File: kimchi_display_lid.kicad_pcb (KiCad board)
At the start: 4 copper layers, 147 x 77 mm, 22 parts, among them J1 DF40HC(3.5)-60DS, J2 DF40HC(3.5)-60DS, J3 H19C-6S-0.5SH, J4 FH19C-40S-0.5SH(10), U1 24C32, U2 AP3019AKTR-G1

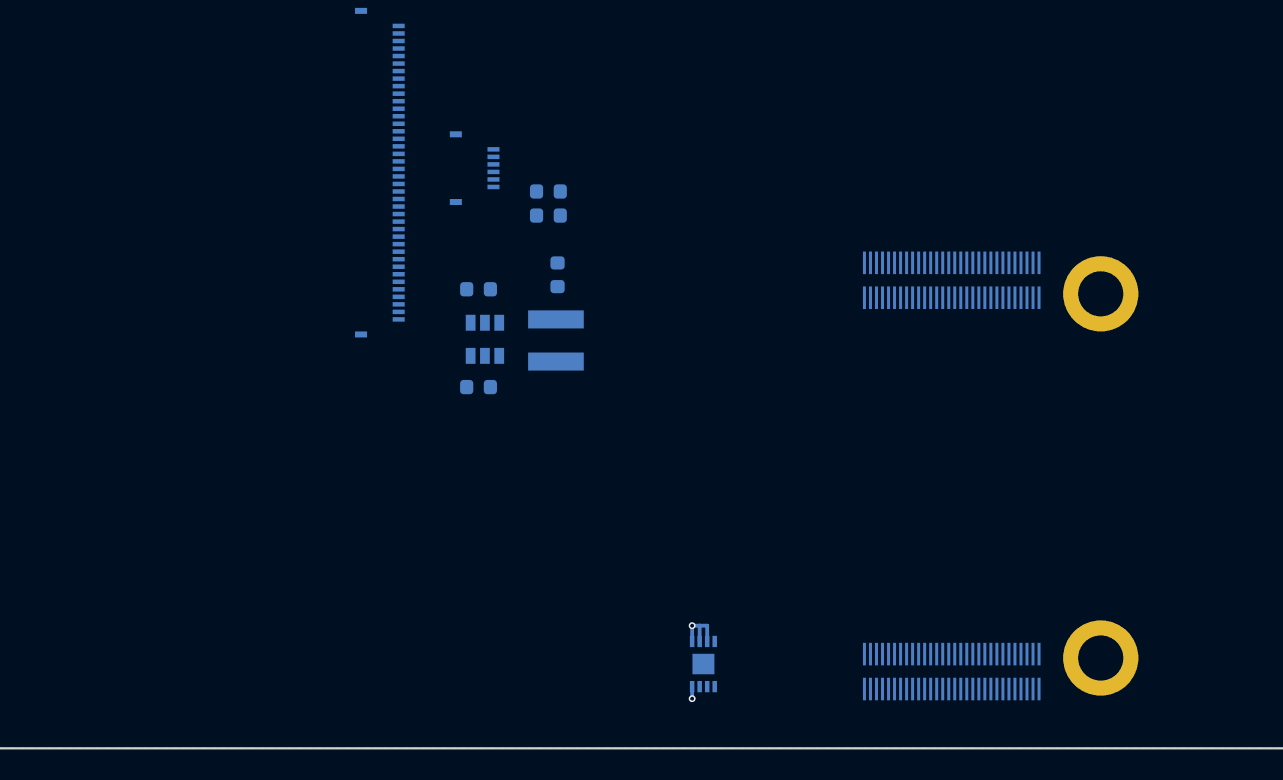
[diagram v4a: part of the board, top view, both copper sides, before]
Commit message: Add level translator and route
Signed-off-by: Michael Welling <mwelling@ieee.org>
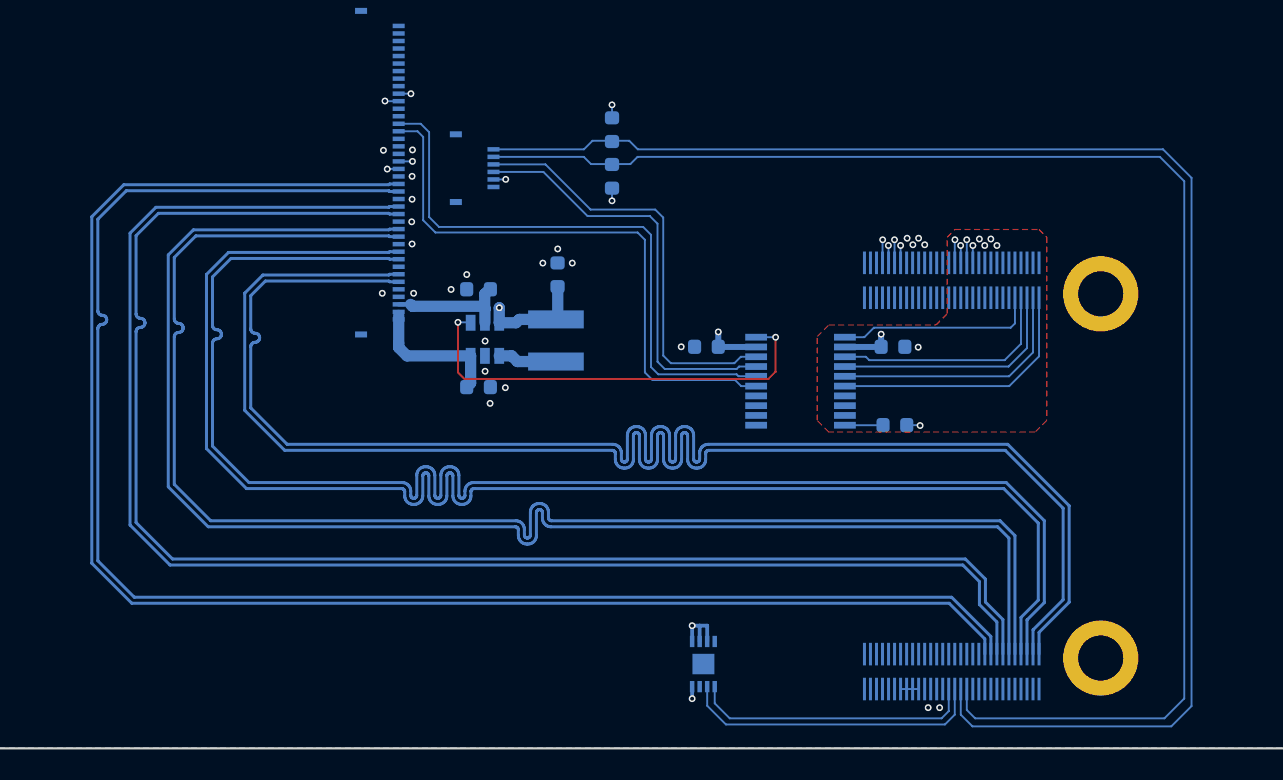
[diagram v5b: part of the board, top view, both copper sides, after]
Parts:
- added C3: .1uF, Capacitor_SMD:C_0603_1608Metric, B.Cu at (144.8, 119.3)
- added C4: .1uF, Capacitor_SMD:C_0603_1608Metric, B.Cu at (132.4, 119.3)
- added R4: 4.7K, Resistor_SMD:R_0603_1608Metric, B.Cu at (144.9, 124.5)
- added U3: TXS0108EPW, Package_SO:TSSOP-20_4.4x6.5mm_P0.65mm, B.Cu at (138.7, 121.6)
- moved R2 7.10 mm to (126.1, 104.9), turned to 270 degrees
- moved R3 4.34 mm to (126.1, 108.0), turned to 90 degrees
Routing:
- net /DISP_D3_N: track 0.00 -> 106.8 mm
- net /DISP_D3_P: track 0.00 -> 106.7 mm
- net /DISP_D2_N: track 0.00 -> 101.3 mm
- net /DISP_D2_P: track 0.00 -> 101.3 mm
- net I2C3_SDA: track 0.00 -> 100.7 mm
- net /DISP_D0_N: track 0.00 -> 100.0 mm
- net /DISP_D1_N: track 0.00 -> 100.0 mm
- net /DISP_CK_N: track 0.00 -> 100.0 mm
- net /DISP_D0_P: track 0.00 -> 100.0 mm
- net /DISP_D1_P: track 0.00 -> 100.0 mm
- net /DISP_CK_P: track 0.00 -> 100.0 mm
- net I2C3_SCL: track 0.00 -> 98.0 mm
- net /LCD_TE: track 0.00 -> 39.2 mm
- net /LCD_RESET: track 0.00 -> 39.2 mm
- net /BL_PWM: track 0.00 -> 29.3 mm, vias 0 -> 2
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- added copper zone on F.Cu, net VDD_1V8

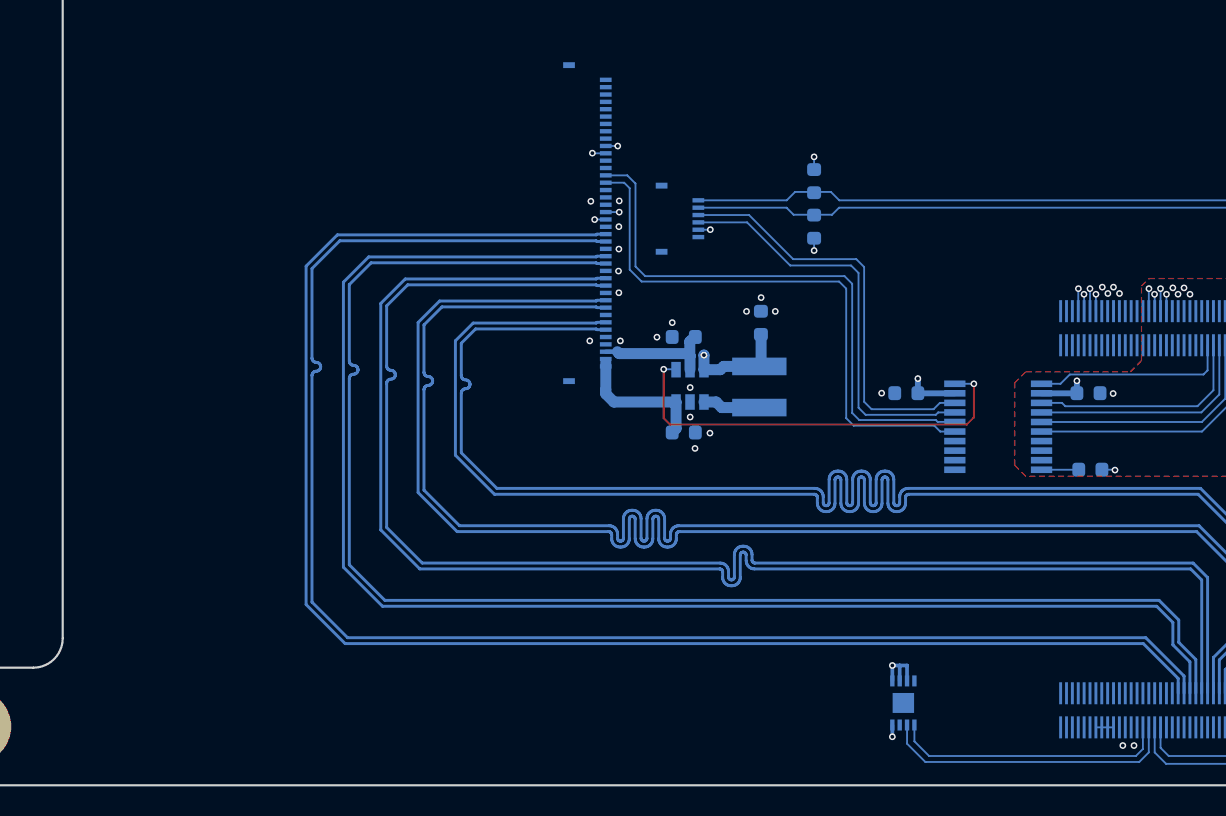
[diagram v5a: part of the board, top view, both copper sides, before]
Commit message: Add USB connector
Signed-off-by: Michael Welling <mwelling@ieee.org>
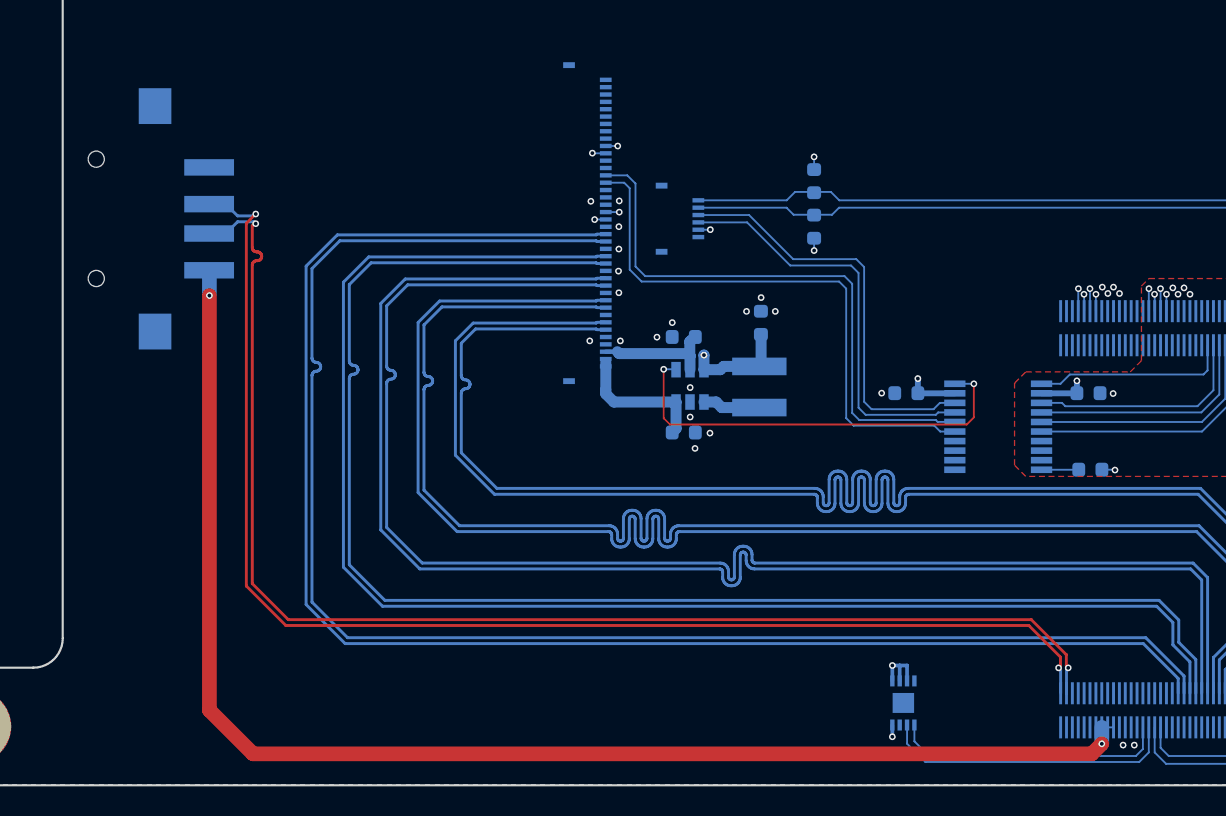
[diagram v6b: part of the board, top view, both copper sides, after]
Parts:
- added J5: USB_A, kimchi_ulid:TE_1-292303-6, B.Cu at (77.3, 107.5)
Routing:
- net VDD_5V: track 1.20 -> 94.5 mm, vias 0 -> 2
- net USB2_DP: track 0.00 -> 89.1 mm, vias 0 -> 2
- net USB2_DN: track 0.00 -> 89.1 mm, vias 0 -> 2

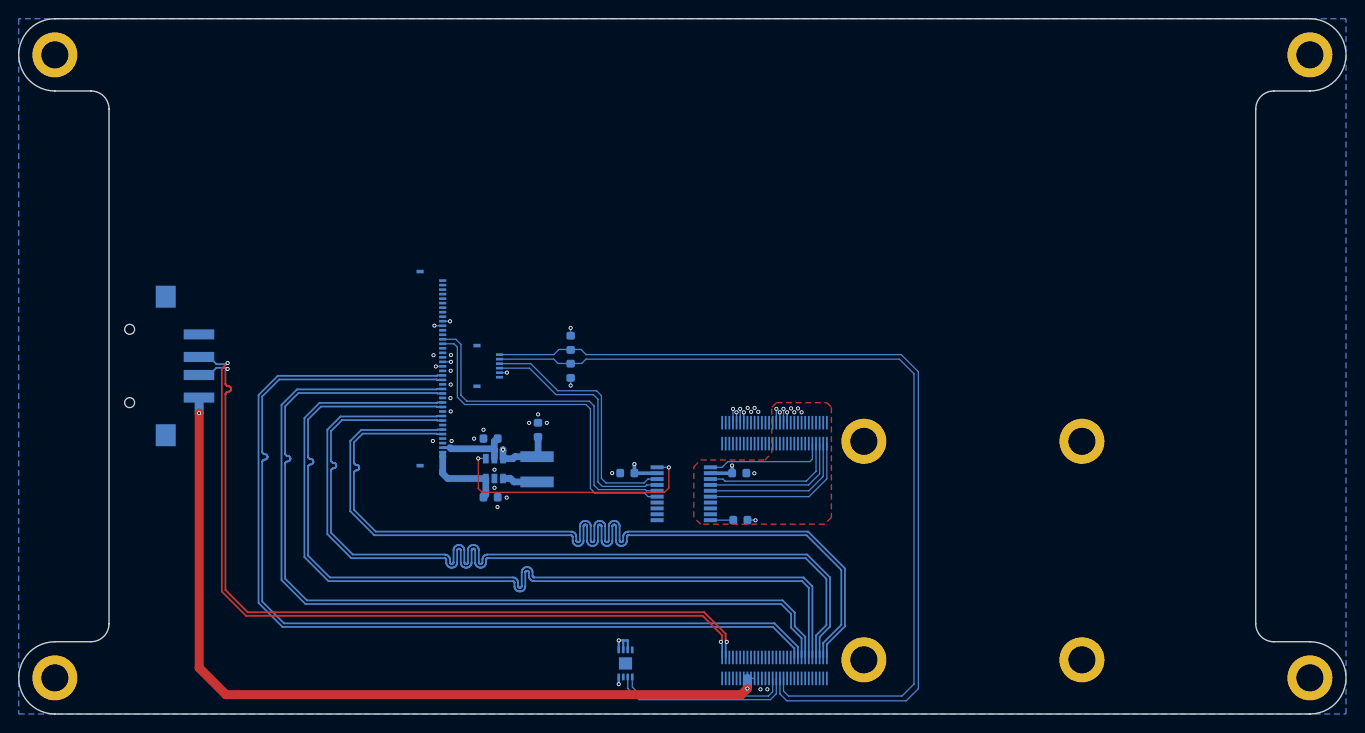
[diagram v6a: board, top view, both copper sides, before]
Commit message: Move USB to opposite side of PCB
It was in the way of the LCD cable on the other side. Doh!

Signed-off-by: Michael Welling <mwelling@ieee.org>
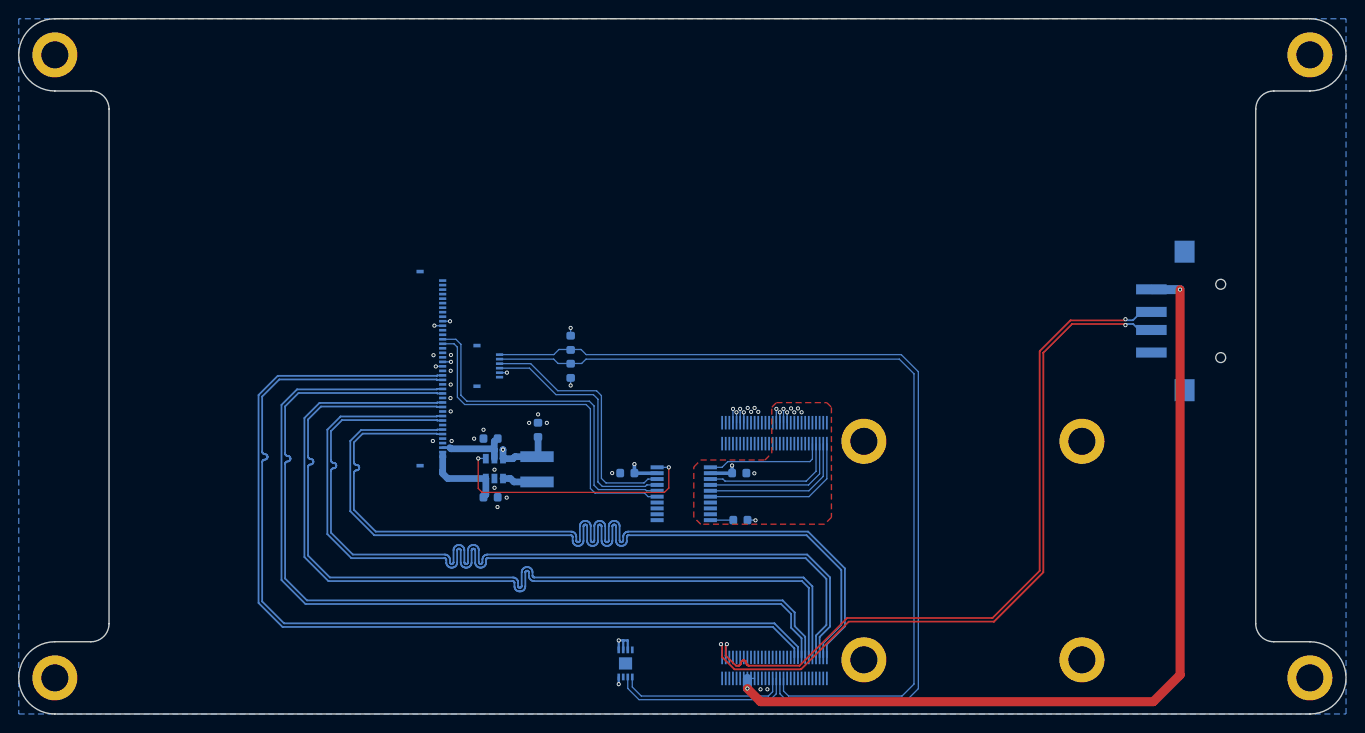
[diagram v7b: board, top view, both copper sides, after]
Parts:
- moved J5 120.9 mm to (198.1, 102.5), turned to 270 degrees
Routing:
- net USB2_DP: track 89.1 -> 81.7 mm
- net USB2_DN: track 89.1 -> 81.9 mm
- net VDD_5V: track 94.5 -> 97.9 mm
